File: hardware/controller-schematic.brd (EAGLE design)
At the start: 38.7 x 25.4 mm, 17 parts, among them IC1 7805TV, Q1 IRLZ44ZV, U1 ATTINY85-20P

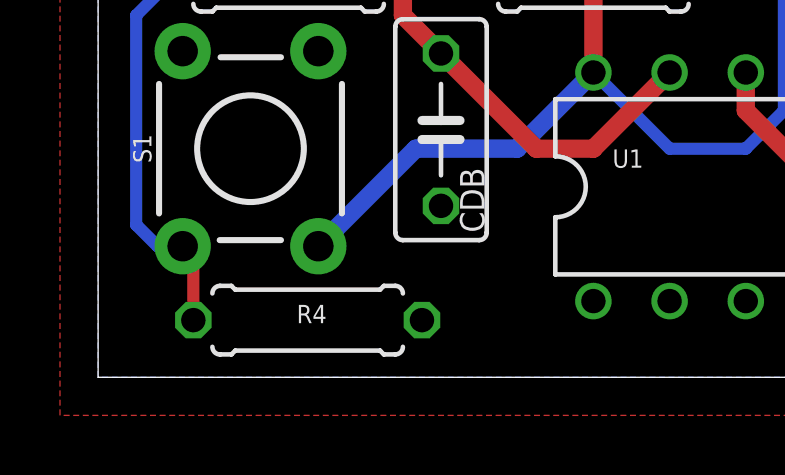
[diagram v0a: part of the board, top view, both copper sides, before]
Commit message: Add passives values to schematic and board
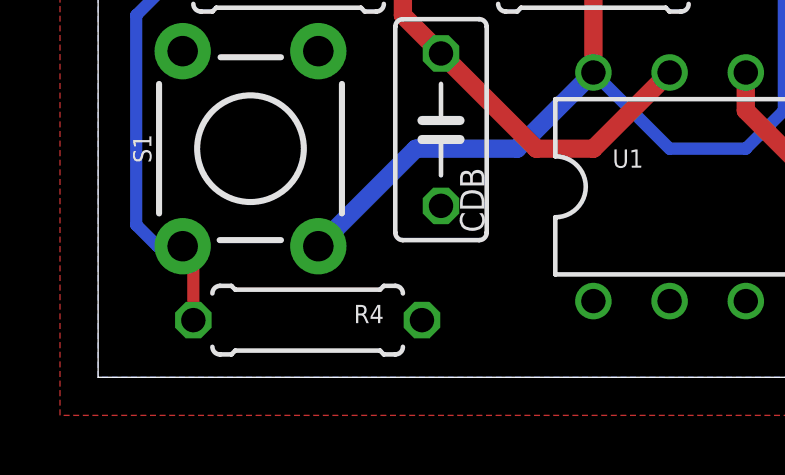
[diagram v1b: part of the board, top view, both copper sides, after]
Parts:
- CB12V, CB5V: value (none) -> 1uF
- CDB: value (none) -> 4.7uF
- R4: value (none) -> 1kΩ
- R5, RG1: value (none) -> 200Ω
- RD: value (none) -> 110Ω
- RG2: value (none) -> 10kΩ
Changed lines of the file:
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@@
 <attribute name="VALUE" x="34.29" y="20.32" size="0.0254" layer="27" rot="R90"/>
 </element>
-<element name="CDB" library="rcl" library_urn="urn:adsk.eagle:library:334" package="C050-030X075" package3d_urn="urn:adsk.eagle:package:23640/1" value="" x="11.43" y="8.255" smashed="yes" rot="R270">
+<element name="CDB" library="rcl" library_urn="urn:adsk.eagle:library:334" package="C050-030X075" package3d_urn="urn:adsk.eagle:package:23640/1" value="4.7uF" x="11.43" y="8.255" smashed="yes" rot="R270">
 <attribute name="NAME" x="12.065" y="6.985" size="0.8128" layer="25" ratio="10" rot="R270"/>
 <attribute name="POPULARITY" value="5" x="-26.67" y="-38.735" size="1.778" layer="27" rot="R270" display="off"/>
 <attribute name="SPICEPREFIX" value="C" x="-26.67" y="-38.735" size="1.778" layer="27" rot="R270" display="off"/>
-<attribute name="VALUE" x="8.382" y="11.811" size="1.27" layer="27" ratio="10" rot="R270"/>
+<attribute name="VALUE" x="11.049" y="3.302" size="0.8128" layer="27" ratio="10"/>
 </element>
 <element name="LED" library="SparkFun-LED" package="LED_3MM" value="" x="28.575" y="5.715" smashed="yes">
@@
 <attribute name="VALUE" x="12.065" y="21.59" size="0.6096" layer="27" ratio="10" rot="R270"/>
 </element>
-<element name="RG1" library="rcl" library_urn="urn:adsk.eagle:library:334" package="0207/7" package3d_urn="urn:adsk.eagle:package:23493/2" value="" x="16.51" y="13.335" smashed="yes" rot="R180">
+<element name="RG1" library="rcl" library_urn="urn:adsk.eagle:library:334" package="0207/7" package3d_urn="urn:adsk.eagle:package:23493/2" value="200Ω" x="16.51" y="13.335" smashed="yes" rot="R180">
 <attribute name="NAME" x="19.05" y="13.208" size="0.6096" layer="25" ratio="10" rot="R180"/>
 <attribute name="POPULARITY" value="22" x="-1.27" y="57.785" size="1.778" layer="27" rot="R180" display="off"/>
 <attribute name="SPICEPREFIX" value="R" x="-1.27" y="57.785" size="1.778" layer="27" rot="R180" display="off"/>
-<attribute name="VALUE" x="18.796" y="13.8938" size="1.27" layer="27" ratio="10" rot="R180"/>
+<attribute name="VALUE" x="16.256" y="13.8938" size="0.8128" layer="27" ratio="10" rot="R180"/>
 </element>
-<element name="RG2" library="rcl" library_urn="urn:adsk.eagle:library:334" package="0207/7" package3d_urn="urn:adsk.eagle:package:23493/2" value="" x="16.51" y="15.875" smashed="yes">
+<element name="RG2" library="rcl" library_urn="urn:adsk.eagle:library:334" package="0207/7" package3d_urn="urn:adsk.eagle:package:23493/2" value="10kΩ" x="16.51" y="15.875" smashed="yes">
 <attribute name="NAME" x="13.97" y="16.002" size="0.6096" layer="25" ratio="10"/>
 <attribute name="POPULARITY" value="22" x="44.45" y="-28.575" size="1.778" layer="27" display="off"/>
 <attribute name="SPICEPREFIX" value="R" x="44.45" y="-28.575" size="1.778" layer="27" display="off"/>
-<attribute name="VALUE" x="14.224" y="15.3162" size="1.27" layer="27" ratio="10"/>
+<attribute name="VALUE" x="16.129" y="15.3162" size="0.8128" layer="27" ratio="10"/>
 </element>
-<element name="RD" library="rcl" library_urn="urn:adsk.eagle:library:334" package="0207/7" package3d_urn="urn:adsk.eagle:package:23493/2" value="" x="33.02" y="1.905" smashed="yes" rot="R180">
+<element name="RD" library="rcl" library_urn="urn:adsk.eagle:library:334" package="0207/7" package3d_urn="urn:adsk.eagle:package:23493/2" value="110Ω" x="33.02" y="1.905" smashed="yes" rot="R180">
 <attribute name="NAME" x="35.56" y="1.778" size="0.6096" layer="25" ratio="10" rot="R180"/>
 <attribute name="POPULARITY" value="22" x="-5.08" y="46.355" size="1.778" layer="27" rot="R180" display="off"/>
 <attribute name="SPICEPREFIX" value="R" x="-5.08" y="46.355" size="1.778" layer="27" rot="R180" display="off"/>
-<attribute name="VALUE" x="35.306" y="2.4638" size="1.27" layer="27" ratio="10" rot="R180"/>
+<attribute name="VALUE" x="32.766" y="2.4638" size="0.8128" layer="27" ratio="10" rot="R180"/>
 </element>
-<element name="R4" library="rcl" library_urn="urn:adsk.eagle:library:334" package="0207/7" package3d_urn="urn:adsk.eagle:package:23493/2" value="" x="6.985" y="1.905" smashed="yes" rot="R180">
-<attribute name="NAME" x="7.62" y="2.413" size="0.6096" layer="25" ratio="10" rot="R180"/>
+<element name="R4" library="rcl" library_urn="urn:adsk.eagle:library:334" package="0207/7" package3d_urn="urn:adsk.eagle:package:23493/2" value="1kΩ" x="6.985" y="1.905" smashed="yes" rot="R180">
+<attribute name="NAME" x="9.525" y="2.413" size="0.6096" layer="25" ratio="10" rot="R180"/>
 <attribute name="POPULARITY" value="22" x="-10.795" y="51.435" size="1.778" layer="27" rot="R180" display="off"/>
 <attribute name="SPICEPREFIX" value="R" x="-10.795" y="51.435" size="1.778" layer="27" rot="R180" display="off"/>
-<attribute name="VALUE" x="9.271" y="2.4638" size="1.27" layer="27" ratio="10" rot="R180"/>
+<attribute name="VALUE" x="6.096" y="1.8288" size="0.8128" layer="27" ratio="10" rot="R180"/>
 </element>
-<element name="R5" library="rcl" library_urn="urn:adsk.eagle:library:334" package="0207/7" package3d_urn="urn:adsk.eagle:package:23493/2" value="" x="6.35" y="13.335" smashed="yes">
+<element name="R5" library="rcl" library_urn="urn:adsk.eagle:library:334" package="0207/7" package3d_urn="urn:adsk.eagle:package:23493/2" value="200Ω" x="6.35" y="13.335" smashed="yes">
 <attribute name="NAME" x="7.62" y="12.827" size="0.6096" layer="25" ratio="10"/>
 <attribute name="POPULARITY" value="22" x="34.29" y="-36.195" size="1.778" layer="27" display="off"/>
 <attribute name="SPICEPREFIX" value="R" x="34.29" y="-36.195" size="1.778" layer="27" display="off"/>
-<attribute name="VALUE" x="4.064" y="12.7762" size="1.27" layer="27" ratio="10"/>
+<attribute name="VALUE" x="4.064" y="12.7762" size="0.8128" layer="27" ratio="10"/>
 </element>
 <element name="S1" library="SparkFun-Switches" package="TACTILE_SWITCH_PTH_6.0MM" value="MOMENTARY-SWITCH-SPST-PTH-6.0MM" x="5.08" y="7.62" smashed="yes" rot="R90">
@@
 <attribute name="VALUE" x="20.32" y="18.415" size="0.6096" layer="27" ratio="10"/>
 </element>
-<element name="CB5V" library="rcl" library_urn="urn:adsk.eagle:library:334" package="C050-030X075" package3d_urn="urn:adsk.eagle:package:23640/1" value="" x="25.4" y="15.24" smashed="yes">
+<element name="CB5V" library="rcl" library_urn="urn:adsk.eagle:library:334" package="C050-030X075" package3d_urn="urn:adsk.eagle:package:23640/1" value="1uF" x="25.4" y="15.24" smashed="yes">
 <attribute name="NAME" x="26.035" y="13.97" size="0.6096" layer="25" ratio="10"/>
 <attribute name="POPULARITY" value="5" x="25.4" y="15.24" size="1.778" layer="27" display="off"/>
 <attribute name="SPICEPREFIX" value="C" x="25.4" y="15.24" size="1.778" layer="27" display="off"/>
-<attribute name="VALUE" x="21.844" y="12.192" size="1.27" layer="27" ratio="10"/>
+<attribute name="VALUE" x="30.353" y="14.859" size="0.8128" layer="27" ratio="10" rot="R90"/>
 </element>
-<element name="CB12V" library="rcl" library_urn="urn:adsk.eagle:library:334" package="C050-030X075" package3d_urn="urn:adsk.eagle:package:23640/1" value="" x="6.35" y="16.51" smashed="yes">
+<element name="CB12V" library="rcl" library_urn="urn:adsk.eagle:library:334" package="C050-030X075" package3d_urn="urn:adsk.eagle:package:23640/1" value="1uF" x="6.35" y="16.51" smashed="yes">
 <attribute name="NAME" x="2.794" y="15.24" size="0.6096" layer="25" ratio="10"/>
 <attribute name="POPULARITY" value="5" x="6.35" y="16.51" size="0.6096" layer="27" display="off"/>
 <attribute name="SPICEPREFIX" value="C" x="6.35" y="16.51" size="0.6096" layer="27" display="off"/>
-<attribute name="VALUE" x="2.794" y="13.462" size="1.27" layer="27" ratio="10"/>
+<attribute name="VALUE" x="2.413" y="15.24" size="0.8128" layer="27" ratio="10" rot="R90"/>
 </element>
 </elements>
